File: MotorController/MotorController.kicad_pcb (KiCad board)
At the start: 2 copper layers, 55 x 45 mm, 44 parts, among them J1 4P4C, J2 AVR-ISP-10, J3 8P8C, J4 Screw_Terminal_01x02, Q1 Q_NMOS_GSD, SW2 SW_Push, U1 LD1117S50TR_SOT223, U2 MAX485E, U3 ATmega8A-AU, Y1 8Mhz

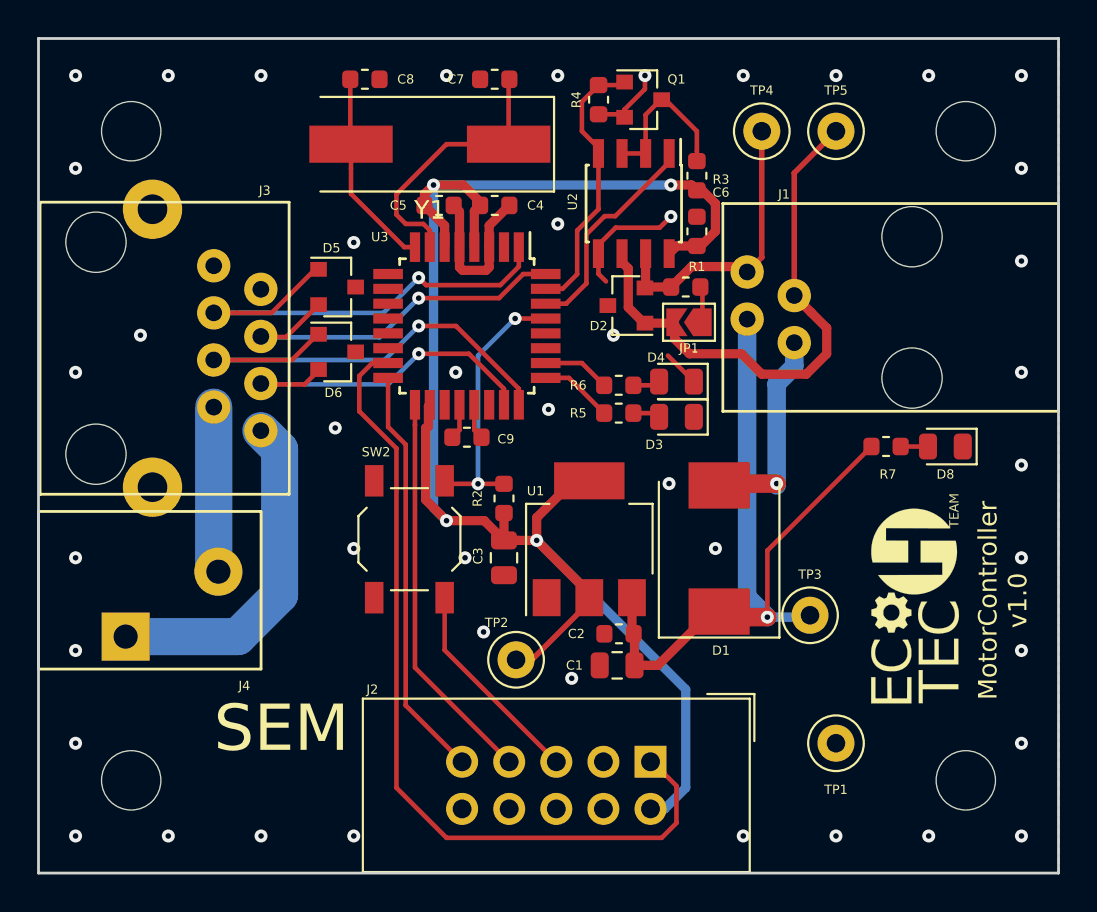
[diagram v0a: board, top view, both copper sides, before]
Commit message: Added version date on silk screen and changed signal tracks width to 0,2.
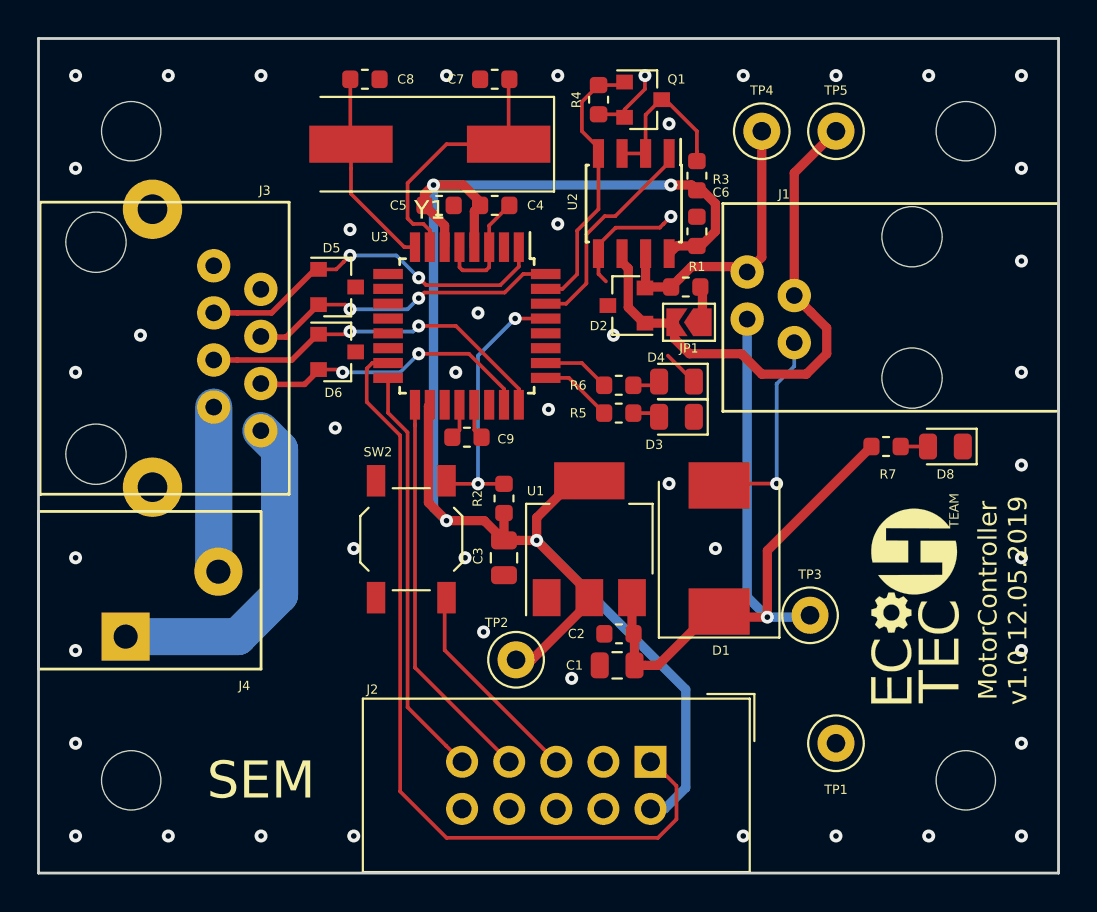
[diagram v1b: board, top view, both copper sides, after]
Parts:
- moved SW2 0.10 mm to (95.1, 87.0)
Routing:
- net /B3: track 25.7 -> 19.5 mm, vias 1 -> 2
- net /B1: track 25.5 -> 19.9 mm, vias 1 -> 2
- net /B2: track 20.7 -> 17.0 mm, vias 1 -> 2
- net /B4: track 18.9 -> 15.5 mm, vias 1 -> 2
- net GND: track 35.3 -> 33.4 mm, vias 45 -> 47
- net Net-(C7-Pad1): track 14.9 -> 14.2 mm
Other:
- net class Default: trace_width 0.25 -> 0.2
- board text added: "MotorController v1.0 12.05.2019"
- board text removed: "MotorController v1.0"
